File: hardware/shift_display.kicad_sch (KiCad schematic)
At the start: 73 parts, among them U10 74HC595, U11 74HC595, U12 SM420561N, U13 SM420561N, U14 SM420561N, U3 74HC595, U4 74HC595, U5 74HC595, U6 SM420561N, U7 SM420561N, U8 SM420561N, U9 74HC595

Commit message: Pre-autoroute on rev2
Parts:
- removed R13, R14, R15, R16, R17, R18, R19, R20, R21, R22, R23, R24, R25, R26, R27, R28, R29, R30, R31, R32, R33, R34, R35, R36, R37, R38, R39, R40, R41, R42, R43, R44, R45, R46, R47, R48, R49, R50, R51, R52, R53, R54, R55, R56, R57, R58, R59, R60: 470R, Resistor_SMD:R_0603_1608Metric, symbol Device:R
- added RN1, RN10, RN11, RN12, RN2, RN3, RN4, RN5, RN6, RN7, RN8, RN9: 220R, Resistor_SMD:R_Array_Convex_4x0603, symbol Device:R_Pack04
- C14: renamed from C12; JLCPCB Part C307331 -> (none); LCSC Part (none) -> C307331; MFR Part CL05B104KB54PNC -> (none)
- C15: JLCPCB Part C307331 -> (none); LCSC Part (none) -> C307331; MFR Part CL05B104KB54PNC -> (none)
- C16: renamed from C13; JLCPCB Part C307331 -> (none); LCSC Part (none) -> C307331; MFR Part CL05B104KB54PNC -> (none)
- C17: renamed from C16; JLCPCB Part C307331 -> (none); LCSC Part (none) -> C307331; MFR Part CL05B104KB54PNC -> (none)
- C18: renamed from C14; JLCPCB Part C307331 -> (none); LCSC Part (none) -> C307331; MFR Part CL05B104KB54PNC -> (none)
- C19: renamed from C17; JLCPCB Part C307331 -> (none); LCSC Part (none) -> C307331; MFR Part CL05B104KB54PNC -> (none)
- R12: renamed from R11; JLCPCB Part C25744 -> (none); LCSC Part (none) -> C25744
- R13: renamed from R12; JLCPCB Part C25744 -> (none); LCSC Part (none) -> C25744
- U10: renamed from U4; JLCPCB Part C5947 -> (none); LCSC Part (none) -> C5947
- U11: renamed from U10; JLCPCB Part C5947 -> (none); LCSC Part (none) -> C5947
- U12: renamed from U8; value SM420561N -> VDMY10C0; footprint Display_7Segment:7SegmentLED_LTS6760_LTS6780 -> Mouser:VDMx10x0; MFR Part 157142B12703 -> VDMY10C0; Mouser Part 710-157142B12703 -> 78-VDMY10C0
- U13: renamed from U14; value SM420561N -> VDMY10C0; footprint Display_7Segment:7SegmentLED_LTS6760_LTS6780 -> Mouser:VDMx10x0; MFR Part 157142B12703 -> VDMY10C0; Mouser Part 710-157142B12703 -> 78-VDMY10C0
- U14: renamed from U5; JLCPCB Part C5947 -> (none); LCSC Part (none) -> C5947
- U15: renamed from U11; JLCPCB Part C5947 -> (none); LCSC Part (none) -> C5947
- U4: renamed from U6; value SM420561N -> VDMY10C0; footprint Display_7Segment:7SegmentLED_LTS6760_LTS6780 -> Mouser:VDMx10x0; MFR Part 157142B12703 -> VDMY10C0; Mouser Part 710-157142B12703 -> 78-VDMY10C0
- U5: renamed from U12; value SM420561N -> VDMY10C0; footprint Display_7Segment:7SegmentLED_LTS6760_LTS6780 -> Mouser:VDMx10x0; MFR Part 157142B12703 -> VDMY10C0; Mouser Part 710-157142B12703 -> 78-VDMY10C0
- U6: renamed from U3; JLCPCB Part C5947 -> (none); LCSC Part (none) -> C5947
- U7: renamed from U9; JLCPCB Part C5947 -> (none); LCSC Part (none) -> C5947
- U8: renamed from U7; value SM420561N -> VDMY10C0; footprint Display_7Segment:7SegmentLED_LTS6760_LTS6780 -> Mouser:VDMx10x0; MFR Part 157142B12703 -> VDMY10C0; Mouser Part 710-157142B12703 -> 78-VDMY10C0
- U9: renamed from U13; value SM420561N -> VDMY10C0; footprint Display_7Segment:7SegmentLED_LTS6760_LTS6780 -> Mouser:VDMx10x0; MFR Part 157142B12703 -> VDMY10C0; Mouser Part 710-157142B12703 -> 78-VDMY10C0
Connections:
- net D1A: now also RN1.4 (R4.1)
- net D1B: now also RN1.3 (R3.1)
- net D1C: now also RN1.2 (R2.1)
- net D1D: now also RN1.1 (R1.1)
- net D1E: now also RN3.4 (R4.1)
- net D1F: now also RN3.3 (R3.1)
- net D1G: now also RN3.2 (R2.1)
- net D1P: now also RN3.1 (R1.1)
- net D2A: now also RN2.4 (R4.1)
- net D2B: now also RN2.3 (R3.1)
- net D2C: now also RN2.2 (R2.1)
- net D2D: now also RN2.1 (R1.1)
- net D2E: now also RN4.4 (R4.1)
- net D2F: now also RN4.3 (R3.1)
- net D2G: now also RN4.2 (R2.1)
- net D2P: now also RN4.1 (R1.1)
- net D3A: now also RN5.4 (R4.1)
- net D3B: now also RN5.3 (R3.1)
- net D3C: now also RN5.2 (R2.1)
- net D3D: now also RN5.1 (R1.1)
- net D3E: now also RN7.4 (R4.1)
- net D3F: now also RN7.3 (R3.1)
- net D3G: now also RN7.2 (R2.1)
- net D3P: now also RN7.1 (R1.1)
- net D4A: now also RN6.4 (R4.1)
- net D4B: now also RN6.3 (R3.1)
- net D4C: now also RN6.2 (R2.1)
- net D4D: now also RN6.1 (R1.1)
- net D4E: now also RN8.4 (R4.1)
- net D4F: now also RN8.3 (R3.1)
- net D4G: now also RN8.2 (R2.1)
- net D4P: now also RN8.1 (R1.1)
- net D5A: now also RN9.4 (R4.1)
- net D5B: now also RN9.3 (R3.1)
- net D5C: now also RN9.2 (R2.1)
- net D5D: now also RN9.1 (R1.1)
- net D5E: now also RN11.4 (R4.1)
- net D5F: now also RN11.3 (R3.1)
- net D5G: now also RN11.2 (R2.1)
- net D5P: now also RN11.1 (R1.1)
- net D6A: now also RN10.4 (R4.1)
- net D6B: now also RN10.3 (R3.1)
- net D6C: now also RN10.2 (R2.1)
- net D6D: now also RN10.1 (R1.1)
- net D6E: now also RN12.4 (R4.1)
- net D6F: now also RN12.3 (R3.1)
- net D6G: now also RN12.2 (R2.1)
- net D6P: now also RN12.1 (R1.1)
- net Q1A: now also RN1.5 (R4.2)
- net Q1B: now also RN1.6 (R3.2)
- net Q1C: now also RN1.7 (R2.2)
- net Q1D: now also RN1.8 (R1.2)
- net Q1E: now also RN3.5 (R4.2)
- net Q1F: now also RN3.6 (R3.2)
- net Q1G: now also RN3.7 (R2.2)
- net Q1H: now also RN3.8 (R1.2)
- net Q2A: now also RN2.5 (R4.2)
- net Q2B: now also RN2.6 (R3.2)
- net Q2C: now also RN2.7 (R2.2)
- net Q2D: now also RN2.8 (R1.2)
- net Q2E: now also RN4.5 (R4.2)
- net Q2F: now also RN4.6 (R3.2)
- net Q2G: now also RN4.7 (R2.2)
- net Q2H: now also RN4.8 (R1.2)
- net Q3A: now also RN5.5 (R4.2)
- net Q3B: now also RN5.6 (R3.2)
- net Q3C: now also RN5.7 (R2.2)
- net Q3D: now also RN5.8 (R1.2)
- net Q3E: now also RN7.5 (R4.2)
- net Q3F: now also RN7.6 (R3.2)
- net Q3G: now also RN7.7 (R2.2)
- net Q3H: now also RN7.8 (R1.2)
- net Q4A: now also RN6.5 (R4.2)
- net Q4B: now also RN6.6 (R3.2)
- net Q4C: now also RN6.7 (R2.2)
- net Q4D: now also RN6.8 (R1.2)
- net Q4E: now also RN8.5 (R4.2)
- net Q4F: now also RN8.6 (R3.2)
- net Q4G: now also RN8.7 (R2.2)
- net Q4H: now also RN8.8 (R1.2)
- net Q5A: now also RN9.5 (R4.2)
- net Q5B: now also RN9.6 (R3.2)
- net Q5C: now also RN9.7 (R2.2)
- net Q5D: now also RN9.8 (R1.2)
- net Q5E: now also RN11.5 (R4.2)
- net Q5F: now also RN11.6 (R3.2)
- net Q5G: now also RN11.7 (R2.2)
- net Q5H: now also RN11.8 (R1.2)
- net Q6A: now also RN10.5 (R4.2)
- net Q6B: now also RN10.6 (R3.2)
- net Q6C: now also RN10.7 (R2.2)
- net Q6D: now also RN10.8 (R1.2)
- net Q6E: now also RN12.5 (R4.2)
- net Q6F: now also RN12.6 (R3.2)
- net Q6G: now also RN12.7 (R2.2)
- net Q6H: now also RN12.8 (R1.2)
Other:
- title: Display Circuit -> STM32 Shift Display
- moved on the sheet: U12, U13, U4, U5, U8, U9

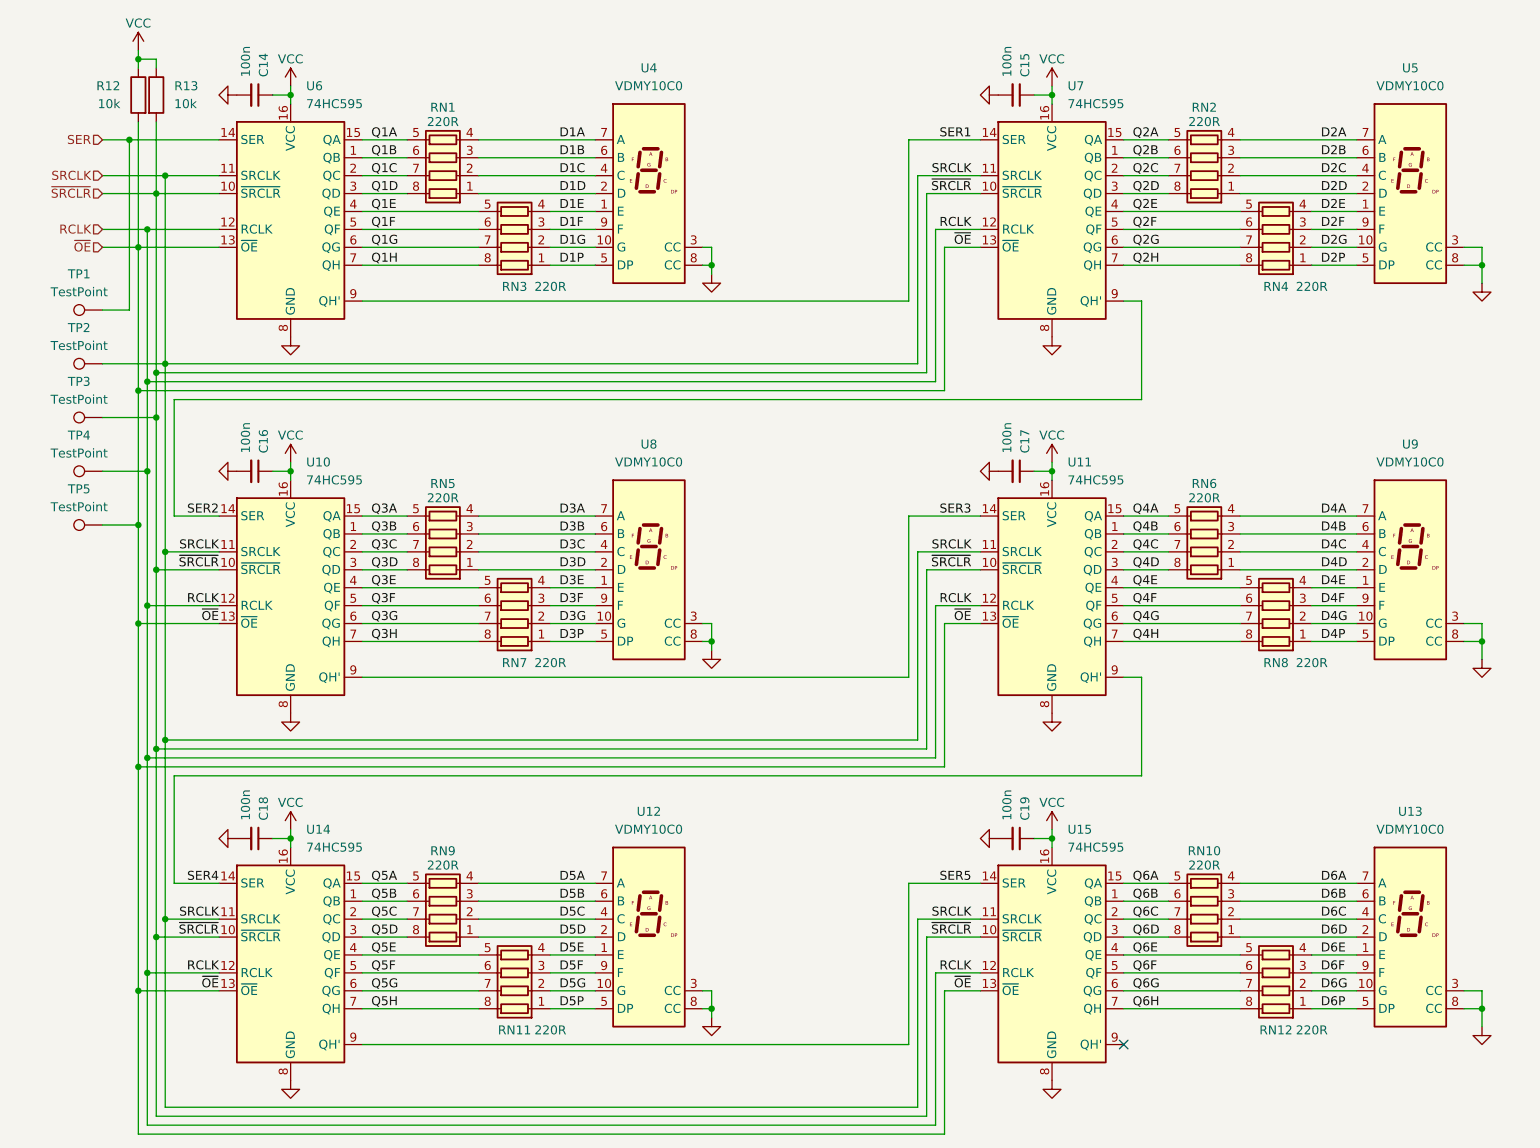
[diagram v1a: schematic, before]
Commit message: Initial rev2 design, layout, routing, and mech done. Order submitted.
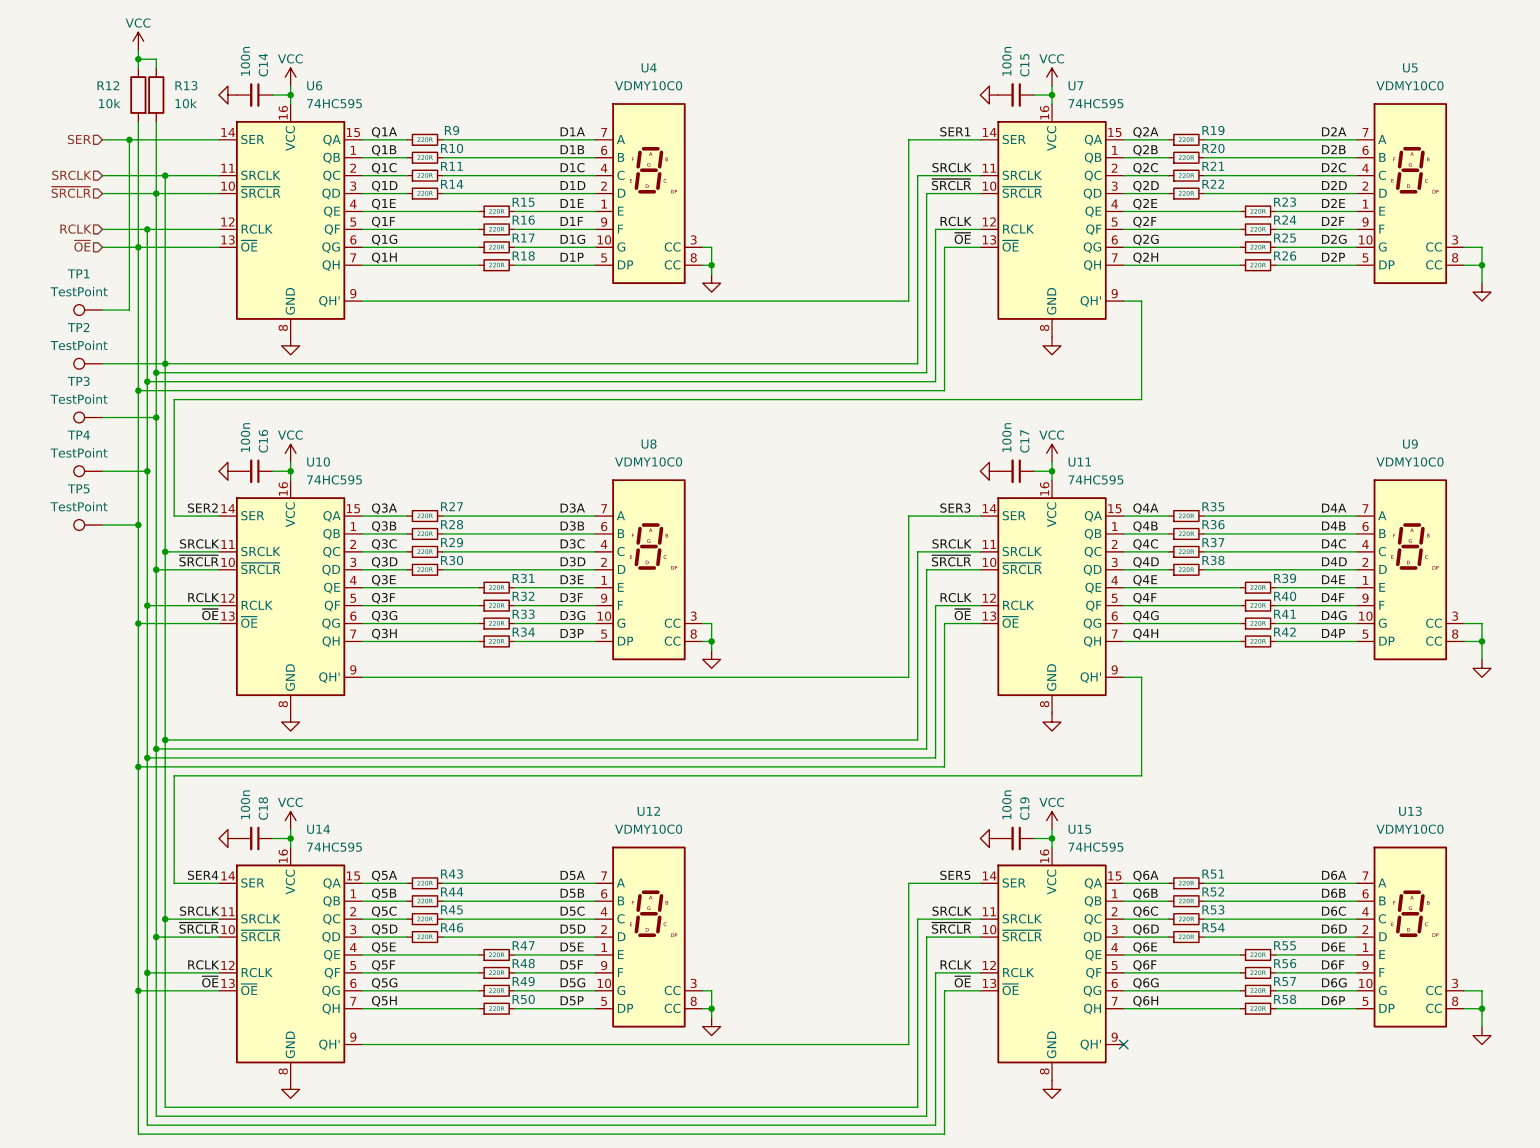
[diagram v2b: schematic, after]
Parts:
- removed RN1, RN10, RN11, RN12, RN2, RN3, RN4, RN5, RN6, RN7, RN8, RN9: 220R, Resistor_SMD:R_Array_Convex_4x0603, symbol Device:R_Pack04
- added R10, R11, R14, R15, R16, R17, R18, R19, R20, R21, R22, R23, R24, R25, R26, R27, R28, R29, R30, R31, R32, R33, R34, R35, R36, R37, R38, R39, R40, R41, R42, R43, R44, R45, R46, R47, R48, R49, R50, R51, R52, R53, R54, R55, R56, R57, R58, R9: 220R, Resistor_SMD:R_0603_1608Metric, symbol Device:R_Small
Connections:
- net D1A: now also R9.2
- net D1B: now also R10.2
- net D1C: now also R11.2
- net D1D: now also R14.2
- net D1E: now also R15.2
- net D1F: now also R16.2
- net D1G: now also R17.2
- net D1P: now also R18.2
- net D2A: now also R19.2
- net D2B: now also R20.2
- net D2C: now also R21.2
- net D2D: now also R22.2
- net D2E: now also R23.2
- net D2F: now also R24.2
- net D2G: now also R25.2
- net D2P: now also R26.2
- net D3A: now also R27.2
- net D3B: now also R28.2
- net D3C: now also R29.2
- net D3D: now also R30.2
- net D3E: now also R31.2
- net D3F: now also R32.2
- net D3G: now also R33.2
- net D3P: now also R34.2
- net D4A: now also R35.2
- net D4B: now also R36.2
- net D4C: now also R37.2
- net D4D: now also R38.2
- net D4E: now also R39.2
- net D4F: now also R40.2
- net D4G: now also R41.2
- net D4P: now also R42.2
- net D5A: now also R43.2
- net D5B: now also R44.2
- net D5C: now also R45.2
- net D5D: now also R46.2
- net D5E: now also R47.2
- net D5F: now also R48.2
- net D5G: now also R49.2
- net D5P: now also R50.2
- net D6A: now also R51.2
- net D6B: now also R52.2
- net D6C: now also R53.2
- net D6D: now also R54.2
- net D6E: now also R55.2
- net D6F: now also R56.2
- net D6G: now also R57.2
- net D6P: now also R58.2
- net Q1A: now also R9.1
- net Q1B: now also R10.1
- net Q1C: now also R11.1
- net Q1D: now also R14.1
- net Q1E: now also R15.1
- net Q1F: now also R16.1
- net Q1G: now also R17.1
- net Q1H: now also R18.1
- net Q2A: now also R19.1
- net Q2B: now also R20.1
- net Q2C: now also R21.1
- net Q2D: now also R22.1
- net Q2E: now also R23.1
- net Q2F: now also R24.1
- net Q2G: now also R25.1
- net Q2H: now also R26.1
- net Q3A: now also R27.1
- net Q3B: now also R28.1
- net Q3C: now also R29.1
- net Q3D: now also R30.1
- net Q3E: now also R31.1
- net Q3F: now also R32.1
- net Q3G: now also R33.1
- net Q3H: now also R34.1
- net Q4A: now also R35.1
- net Q4B: now also R36.1
- net Q4C: now also R37.1
- net Q4D: now also R38.1
- net Q4E: now also R39.1
- net Q4F: now also R40.1
- net Q4G: now also R41.1
- net Q4H: now also R42.1
- net Q5A: now also R43.1
- net Q5B: now also R44.1
- net Q5C: now also R45.1
- net Q5D: now also R46.1
- net Q5E: now also R47.1
- net Q5F: now also R48.1
- net Q5G: now also R49.1
- net Q5H: now also R50.1
- net Q6A: now also R51.1
- net Q6B: now also R52.1
- net Q6C: now also R53.1
- net Q6D: now also R54.1
- net Q6E: now also R55.1
- net Q6F: now also R56.1
- net Q6G: now also R57.1
- net Q6H: now also R58.1
